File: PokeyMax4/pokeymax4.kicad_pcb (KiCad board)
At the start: 2 copper layers, 20.7 x 52.8 mm, 39 parts, among them CN1 18nF, U1 TSV854IQ4T, U2 SN74CB3T16211SM, U3 MAX10, U4 SN74CB3T16211SM, X1 ASE

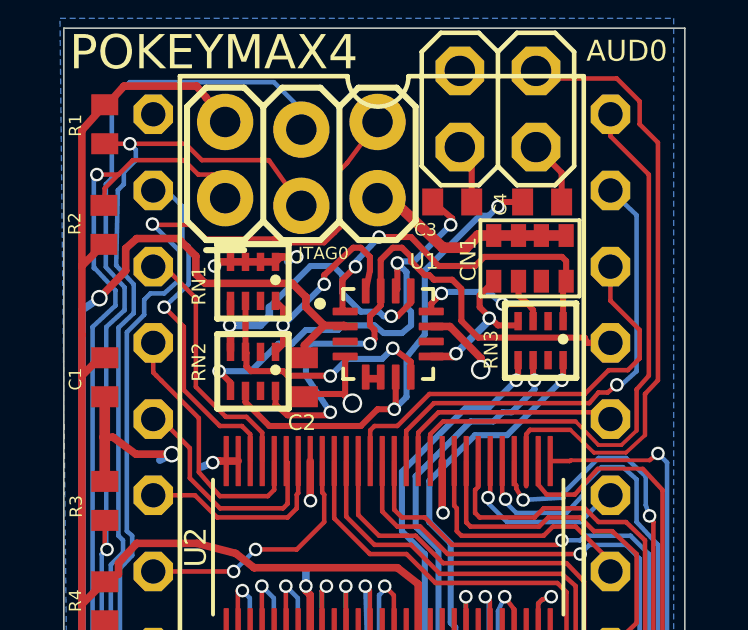
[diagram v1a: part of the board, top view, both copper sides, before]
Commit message: Updates for JLCPCB fabrication and parts library
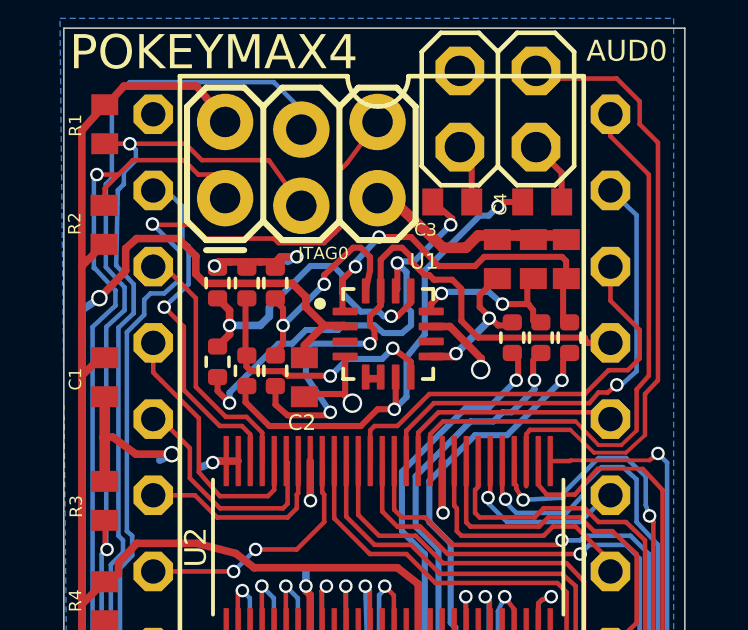
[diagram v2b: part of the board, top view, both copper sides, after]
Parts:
- removed CN1: 18nF, pokeymax4:R1206-8
- removed RN1: 20K, pokeymax4:741-8
- removed RN2: 10K, pokeymax4:741-8
- removed RN3: 560, pokeymax4:741-8
- added C13: 18nF, pokeymax4:C0402, F.Cu at (152.6, 86.3)
- added C14: 18nF, pokeymax4:C0402, F.Cu at (153.8, 86.3)
- added C15: 18nF, pokeymax4:C0402, F.Cu at (154.9, 86.3)
- added R11: 560R, Resistor_SMD:R_0402_1005Metric, F.Cu at (153.1, 88.9)
- added R12: 560R, Resistor_SMD:R_0402_1005Metric, F.Cu at (154.1, 88.9)
- added R13: 560R, Resistor_SMD:R_0402_1005Metric, F.Cu at (155.0, 88.9)
- added R14: 10k, Resistor_SMD:R_0402_1005Metric, F.Cu at (145.2, 90.0)
- added R15: 10k, Resistor_SMD:R_0402_1005Metric, F.Cu at (144.2, 90.0)
- added R16: 10k, Resistor_SMD:R_0402_1005Metric, F.Cu at (143.3, 89.7)
- added R17: 20k, Resistor_SMD:R_0402_1005Metric, F.Cu at (145.2, 87.1)
- added R18: 20k, Resistor_SMD:R_0402_1005Metric, F.Cu at (144.2, 87.1)
- added R19: 20k, Resistor_SMD:R_0402_1005Metric, F.Cu at (143.3, 87.1)
- AUD0: value (none) -> PINHD-2X2
- FB1: value (none) -> R-EU_R0402
- JP1: value (none) -> PINHD-2X5
- JTAG0: value (none) -> CONN_03X2LOCK
- POKEYMAX4: value (none) -> DIL40
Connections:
- net AUDF2 renamed Net-(U1-IN2-)
- net AUDF3 renamed /Audio filter/AUDF3
- net AUDF4 renamed /Audio filter/AUDF4
- net CONF_DONE renamed Net-(U3-CONF_DONE)
- net FAKE_CLK renamed Net-(U3-CLK2)
- net LVLA0 renamed /Level conv/LVLA0
- net LVLA1 renamed /Level conv/LVLA1
- net LVLA10 renamed /Level conv/LVLA10
- net LVLA11 renamed /Level conv/LVLA11
- net LVLA12 renamed /Level conv/LVLA12
- net LVLA13 renamed /Level conv/LVLA13
- net LVLA14 renamed /Level conv/LVLA14
- net LVLA15 renamed /Level conv/LVLA15
- net LVLA16 renamed /Level conv/LVLA16
- net LVLA17 renamed /Level conv/LVLA17
- net LVLA18 renamed /Level conv/LVLA18
- net LVLA19 renamed /Level conv/LVLA19
- net LVLA2 renamed /Level conv/LVLA2
- net LVLA20 renamed /Level conv/LVLA20
- net LVLA22 renamed /Level conv/LVLA22
- net LVLA23 renamed /Level conv/LVLA23
- net LVLA3 renamed /Level conv/LVLA3
- net LVLA4 renamed /Level conv/LVLA4
- net LVLA5 renamed /Level conv/LVLA5
- net LVLA6 renamed /Level conv/LVLA6
- net LVLA7 renamed /Level conv/LVLA7
- net LVLA8 renamed /Level conv/LVLA8
- net LVLA9 renamed /Level conv/LVLA9
- net LVLB0 renamed /Level conv/LVLB0
- net LVLB1 renamed /Level conv/LVLB1
- net LVLB10 renamed /Level conv/LVLB10
- net LVLB11 renamed /Level conv/LVLB11
- net LVLB12 renamed /Level conv/LVLB12
- net LVLB13 renamed /Level conv/LVLB13
- net LVLB14 renamed /Level conv/LVLB14
- net LVLB15 renamed /Level conv/LVLB15
- net LVLB16 renamed /Level conv/LVLB16
- net LVLB17 renamed /Level conv/LVLB17
- net LVLB18 renamed /Level conv/LVLB18
- net LVLB19 renamed /Level conv/LVLB19
- net LVLB2 renamed /Level conv/LVLB2
- net LVLB23 renamed /Level conv/LVLB23
- net LVLB3 renamed /Level conv/LVLB3
- net LVLB4 renamed /Level conv/LVLB4
- net LVLB5 renamed /Level conv/LVLB5
- net LVLB6 renamed /Level conv/LVLB6
- net LVLB7 renamed /Level conv/LVLB7
- net LVLB8 renamed /Level conv/LVLB8
- net NC1 renamed /FPGA/NC1
- net NSTATUS renamed Net-(U3-NSTATUS)
- net OSC_CLOCK renamed /FPGA/OSC_CLOCK
- net TCK renamed /FPGA/TCK
- net TDI renamed /FPGA/TDI
- net TDO renamed /FPGA/TDO
- net TMS renamed /FPGA/TMS
- POKEYMAX4 pad 18: LVLB22 -> 5V0
- POKEYMAX4 pad 19: LVLB21 -> 5V0
- POKEYMAX4 pad 20: LVLB20 -> 5V0
- U1 pad 1: AMPIN1P -> Net-(U1-IN1+)
- U1 pad 12: AMPIN4P -> Net-(U1-IN4+)
- U1 pad 16: AMPIN1M -> Net-(U1-IN1-)
- U1 pad 8: AMPIN3M -> Net-(U1-IN3-)
- U1 pad 9: AMPIN3P -> Net-(U1-IN3+)
- U3 pad C1: (no net) -> unconnected-(U3-TB$1-PadC1)
- U3 pad C11: (no net) -> unconnected-(U3-TB$7-PadC11)
- U3 pad C13: (no net) -> unconnected-(U3-TB$11-PadC13)
- U3 pad C2: (no net) -> unconnected-(U3-TB$3-PadC2)
- U3 pad D1: (no net) -> unconnected-(U3-TB$2-PadD1)
- U3 pad D11: (no net) -> unconnected-(U3-TB$8-PadD11)
- U3 pad D12: (no net) -> unconnected-(U3-TB$10-PadD12)
- U3 pad D2: (no net) -> unconnected-(U3-NC-PadD2)
- U3 pad D3: (no net) -> unconnected-(U3-NC-PadD3)
- U3 pad D6: (no net) -> unconnected-(U3-CRC_ERROR-PadD6)
- U3 pad D7: (no net) -> unconnected-(U3-CONFIG_SEL-PadD7)
- U3 pad E1: (no net) -> Net-(U3-IO_UNUSED-PadE1)
- U3 pad E10: (no net) -> Net-(U3-IO_UNUSED-PadE1)
- U3 pad E12: (no net) -> Net-(U3-IO_UNUSED-PadE1)
- U3 pad E2: (no net) -> unconnected-(U3-NC-PadE2)
- U3 pad E3: (no net) -> Net-(U3-IO_UNUSED-PadE1)
- U3 pad E4: (no net) -> Net-(U3-IO_UNUSED-PadE1)
- U3 pad E5: (no net) -> unconnected-(U3-JTAG_EN-PadE5)
- U3 pad E6: (no net) -> Net-(U3-IO_UNUSED-PadE1)
- U3 pad E8: (no net) -> Net-(U3-IO_UNUSED-PadE1)
- U3 pad E9: (no net) -> Net-(U3-IO_UNUSED-PadE1)
- U3 pad F1: (no net) -> Net-(U3-IO_UNUSED-PadE1)
- U3 pad F10: (no net) -> Net-(U3-IO_UNUSED-PadE1)
- U3 pad F12: (no net) -> Net-(U3-IO_UNUSED-PadE1)
- U3 pad F4: (no net) -> Net-(U3-IO_UNUSED-PadE1)
- U3 pad F8: (no net) -> Net-(U3-IO_UNUSED-PadE1)
- U3 pad F9: (no net) -> Net-(U3-IO_UNUSED-PadE1)
- U3 pad G10: (no net) -> Net-(U3-IO_UNUSED-PadE1)
- U3 pad G4: (no net) -> Net-(U3-IO_UNUSED-PadE1)
- U3 pad G5: (no net) -> Net-(U3-IO_UNUSED-PadE1)
- U3 pad H1: (no net) -> Net-(U3-IO_UNUSED-PadE1)
- U3 pad H10: (no net) -> Net-(U3-IO_UNUSED-PadE1)
- U3 pad H2: (no net) -> Net-(U3-IO_UNUSED-PadE1)
- U3 pad H3: (no net) -> Net-(U3-IO_UNUSED-PadE1)
- U3 pad H4: (no net) -> unconnected-(U3-CLK1-PadH4)
- U3 pad H5: (no net) -> Net-(U3-IO_UNUSED-PadE1)
- U3 pad H6: (no net) -> unconnected-(U3-CLK0-PadH6)
- U3 pad H9: (no net) -> Net-(U3-IO_UNUSED-PadE1)
- U3 pad J1: (no net) -> Net-(U3-IO_UNUSED-PadE1)
- U3 pad J10: (no net) -> Net-(U3-IO_UNUSED-PadE1)
- U3 pad J2: (no net) -> Net-(U3-IO_UNUSED-PadE1)
- U3 pad J5: (no net) -> unconnected-(U3-BB$20-PadJ5)
- U3 pad J6: (no net) -> unconnected-(U3-BB$21-PadJ6)
- U3 pad J7: (no net) -> unconnected-(U3-BB$22-PadJ7)
- U3 pad J8: (no net) -> unconnected-(U3-BB$23-PadJ8)
- U3 pad J9: (no net) -> Net-(U3-IO_UNUSED-PadE1)
- U3 pad K10: (no net) -> unconnected-(U3-BB$12-PadK10)
- U3 pad K11: (no net) -> unconnected-(U3-BB$14-PadK11)
- U3 pad K2: (no net) -> unconnected-(U3-BB$3-PadK2)
- U3 pad K5: (no net) -> unconnected-(U3-BB$7-PadK5)
- U3 pad K6: (no net) -> unconnected-(U3-BB$9-PadK6)
- U3 pad K7: (no net) -> unconnected-(U3-BB$10-PadK7)
- U3 pad K8: (no net) -> unconnected-(U3-BB$11-PadK8)
- U3 pad L2: (no net) -> unconnected-(U3-BB$4-PadL2)
- U3 pad N11: (no net) -> unconnected-(U3-B$20-PadN11)
- U3 pad N12: (no net) -> unconnected-(U3-B$22-PadN12)
- U3 pad N2: (no net) -> unconnected-(U3-B$3-PadN2)
- U3 pad N3: (no net) -> unconnected-(U3-B$5-PadN3)
- U4 pad 30: LVLB22 -> 5V0
- U4 pad 31: LVLB21 -> 5V0
- U4 pad 32: LVLB20 -> 5V0
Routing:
- net 5V0: track 68.1 -> 94.2 mm, vias 4 -> 5
- net Net-(U1-IN1+): track 0.00 -> 11.9 mm, vias 0 -> 2
- net AMPIN1P: track 11.9 -> 0.00 mm, vias 2 -> 0
- net LVLB20: track 11.7 -> 0.00 mm, vias 1 -> 0
- net Net-(U1-IN3-): track 0.00 -> 8.85 mm, vias 0 -> 2
- net AMPIN3M: track 8.85 -> 0.00 mm, vias 2 -> 0
- net LVLB21: track 8.64 -> 0.00 mm
- net Net-(U1-IN1-): track 0.00 -> 7.32 mm, vias 0 -> 2
- net AMPIN1M: track 7.32 -> 0.00 mm, vias 2 -> 0
- net LVLB22: track 5.84 -> 0.00 mm
- net AMPIN4P: track 5.35 -> 0.00 mm, vias 2 -> 0
- net Net-(U1-IN3+): track 0.00 -> 5.28 mm, vias 0 -> 2
- net AMPIN3P: track 5.28 -> 0.00 mm, vias 2 -> 0
- net Net-(U1-IN4+): track 0.00 -> 4.92 mm, vias 0 -> 2
- net Net-(U1-OUT4): track 14.9 -> 15.4 mm

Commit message: Final adjustements to production files for JLC
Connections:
- POKEYMAX4 pad 18: 5V0 -> /Level conv/LVLB22
- POKEYMAX4 pad 19: 5V0 -> /Level conv/LVLB21
- POKEYMAX4 pad 20: 5V0 -> /Level conv/LVLB20
- U3 pad E1: Net-(U3-IO_UNUSED-PadE1) -> unconnected-(U3-IO_UNUSED-PadE1)_21
- U3 pad E10: Net-(U3-IO_UNUSED-PadE1) -> unconnected-(U3-IO_UNUSED-PadE1)_2
- U3 pad E12: Net-(U3-IO_UNUSED-PadE1) -> unconnected-(U3-IO_UNUSED-PadE1)_13
- U3 pad E3: Net-(U3-IO_UNUSED-PadE1) -> unconnected-(U3-IO_UNUSED-PadE1)_17
- U3 pad E4: Net-(U3-IO_UNUSED-PadE1) -> unconnected-(U3-IO_UNUSED-PadE1)_10
- U3 pad E6: Net-(U3-IO_UNUSED-PadE1) -> unconnected-(U3-IO_UNUSED-PadE1)_6
- U3 pad E8: Net-(U3-IO_UNUSED-PadE1) -> unconnected-(U3-IO_UNUSED-PadE1)_12
- U3 pad E9: Net-(U3-IO_UNUSED-PadE1) -> unconnected-(U3-IO_UNUSED-PadE1)_19
- U3 pad F1: Net-(U3-IO_UNUSED-PadE1) -> unconnected-(U3-IO_UNUSED-PadE1)_24
- U3 pad F10: Net-(U3-IO_UNUSED-PadE1) -> unconnected-(U3-IO_UNUSED-PadE1)_4
- U3 pad F12: Net-(U3-IO_UNUSED-PadE1) -> unconnected-(U3-IO_UNUSED-PadE1)_1
- U3 pad F4: Net-(U3-IO_UNUSED-PadE1) -> unconnected-(U3-IO_UNUSED-PadE1)_8
- U3 pad F8: Net-(U3-IO_UNUSED-PadE1) -> unconnected-(U3-IO_UNUSED-PadE1)_9
- U3 pad F9: Net-(U3-IO_UNUSED-PadE1) -> unconnected-(U3-IO_UNUSED-PadE1)_18
- U3 pad G10: Net-(U3-IO_UNUSED-PadE1) -> unconnected-(U3-IO_UNUSED-PadE1)_15
- U3 pad G4: Net-(U3-IO_UNUSED-PadE1) -> unconnected-(U3-IO_UNUSED-PadE1)_16
- U3 pad G5: Net-(U3-IO_UNUSED-PadE1) -> unconnected-(U3-IO_UNUSED-PadE1)_22
- U3 pad H1: Net-(U3-IO_UNUSED-PadE1) -> unconnected-(U3-IO_UNUSED-PadE1)_3
- U3 pad H10: Net-(U3-IO_UNUSED-PadE1) -> unconnected-(U3-IO_UNUSED-PadE1)_11
- U3 pad H2: Net-(U3-IO_UNUSED-PadE1) -> unconnected-(U3-IO_UNUSED-PadE1)_25
- U3 pad H3: Net-(U3-IO_UNUSED-PadE1) -> unconnected-(U3-IO_UNUSED-PadE1)_23
- U3 pad H5: Net-(U3-IO_UNUSED-PadE1) -> unconnected-(U3-IO_UNUSED-PadE1)_5
- U3 pad H9: Net-(U3-IO_UNUSED-PadE1) -> unconnected-(U3-IO_UNUSED-PadE1)_7
- U3 pad J1: Net-(U3-IO_UNUSED-PadE1) -> unconnected-(U3-IO_UNUSED-PadE1)
- U3 pad J10: Net-(U3-IO_UNUSED-PadE1) -> unconnected-(U3-IO_UNUSED-PadE1)_20
- U3 pad J2: Net-(U3-IO_UNUSED-PadE1) -> unconnected-(U3-IO_UNUSED-PadE1)_26
- U3 pad J9: Net-(U3-IO_UNUSED-PadE1) -> unconnected-(U3-IO_UNUSED-PadE1)_14
- U4 pad 30: 5V0 -> /Level conv/LVLB22
- U4 pad 31: 5V0 -> /Level conv/LVLB21
- U4 pad 32: 5V0 -> /Level conv/LVLB20
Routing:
- net 5V0: track 94.2 -> 68.1 mm, vias 5 -> 4
- net /Level conv/LVLB20: track 0.00 -> 11.7 mm, vias 0 -> 1
- net /Level conv/LVLB21: track 0.00 -> 8.64 mm
- net /Level conv/LVLB22: track 0.00 -> 5.84 mm
